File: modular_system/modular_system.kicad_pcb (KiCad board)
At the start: 2 copper layers, 96.8 x 48.5 mm, 12 parts, among them J1 Screw_Terminal_01x02, J2 Conn_01x01_Male, J3 Conn_01x01_Male, J4 Conn_01x01_Male, J5 Conn_01x01_Male, J6 Conn_01x04_Female, J7 Conn_01x04_Female, U1 BluePill_STM32F103C

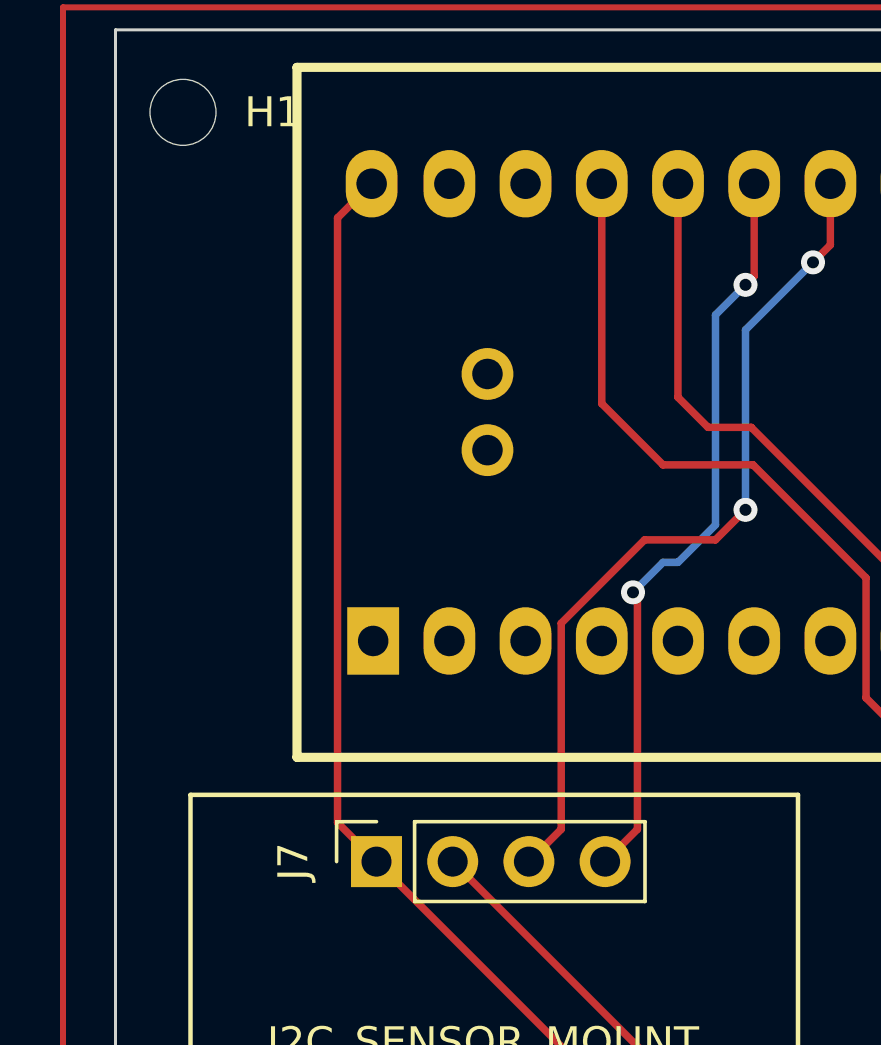
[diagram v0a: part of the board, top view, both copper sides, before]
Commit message: added extra ground trace
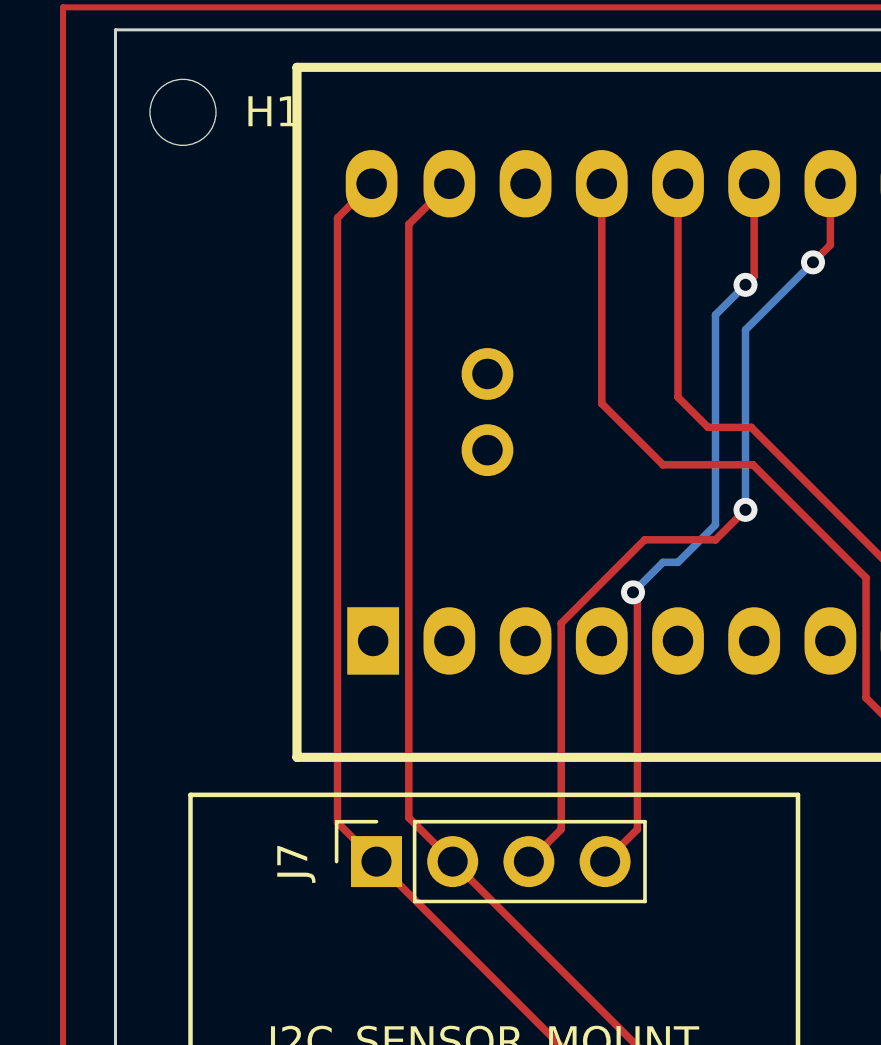
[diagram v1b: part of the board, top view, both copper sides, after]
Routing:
- net GND: track 126.8 -> 150.5 mm
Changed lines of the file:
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@@
   (segment (start 108.901089 56.767311) (end 110.0384 55.63) (width 0.25) (layer "F.Cu") (net 2))
   (segment (start 148.35 88.98) (end 120.955 88.98) (width 0.25) (layer "F.Cu") (net 2))
+  (segment (start 111.277311 56.981889) (end 111.277311 76.762311) (width 0.25) (layer "F.Cu") (net 3))
   (segment (start 134.77 91.52) (end 134.75 91.5) (width 0.25) (layer "F.Cu") (net 3))
   (segment (start 158.3492 75.8492) (end 158.5 76) (width 0.25) (layer "F.Cu") (net 3))
@@
   (segment (start 165.75 81.5) (end 176 71.25) (width 0.25) (layer "F.Cu") (net 3))
   (segment (start 148.35 91.52) (end 155.73 91.52) (width 0.25) (layer "F.Cu") (net 3))
+  (segment (start 112.6292 55.63) (end 111.277311 56.981889) (width 0.25) (layer "F.Cu") (net 3))
+  (segment (start 111.277311 76.762311) (end 112.74 78.225) (width 0.25) (layer "F.Cu") (net 3))
   (segment (start 177.035 56.215) (end 179.055 56.215) (width 0.25) (layer "F.Cu") (net 3))
   (segment (start 165.75 81.5) (end 162 81.5) (width 0.25) (layer "F.Cu") (net 3))

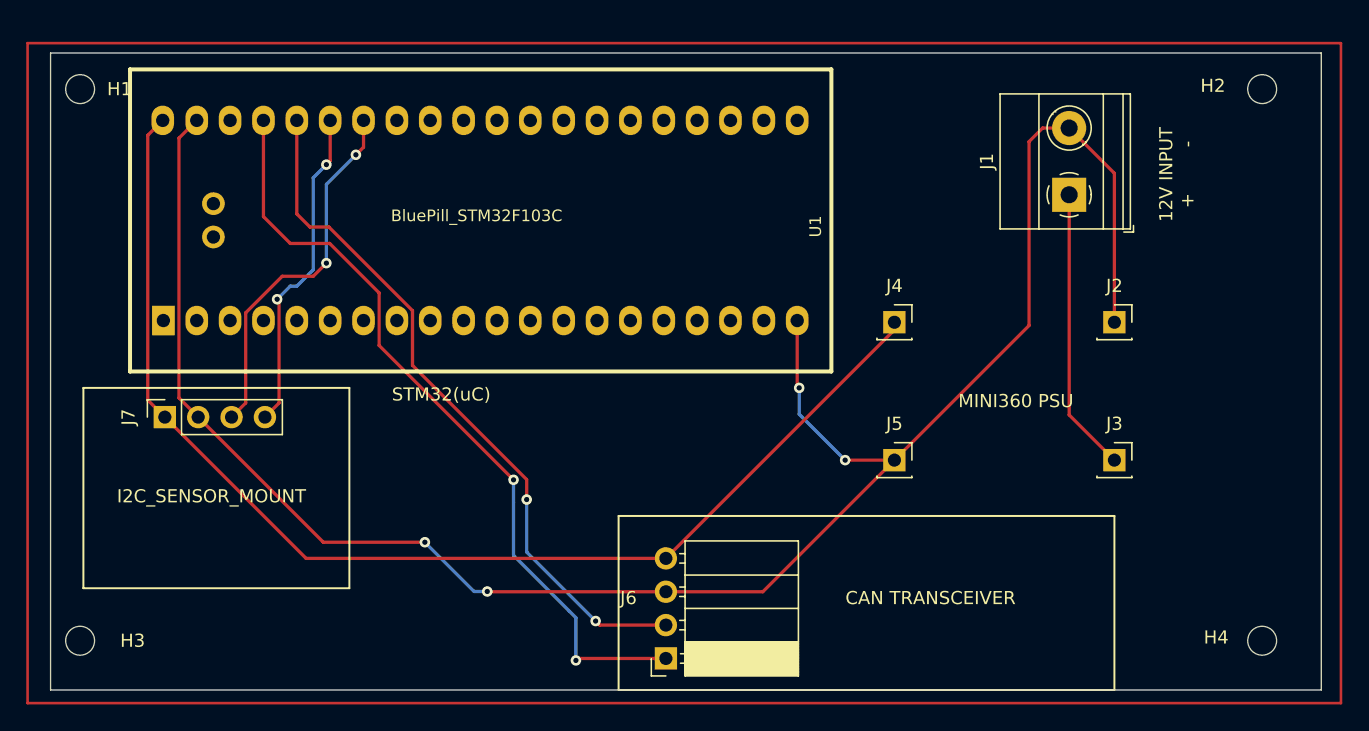
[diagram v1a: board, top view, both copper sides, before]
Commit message: updated with new labels and text on silkscreen
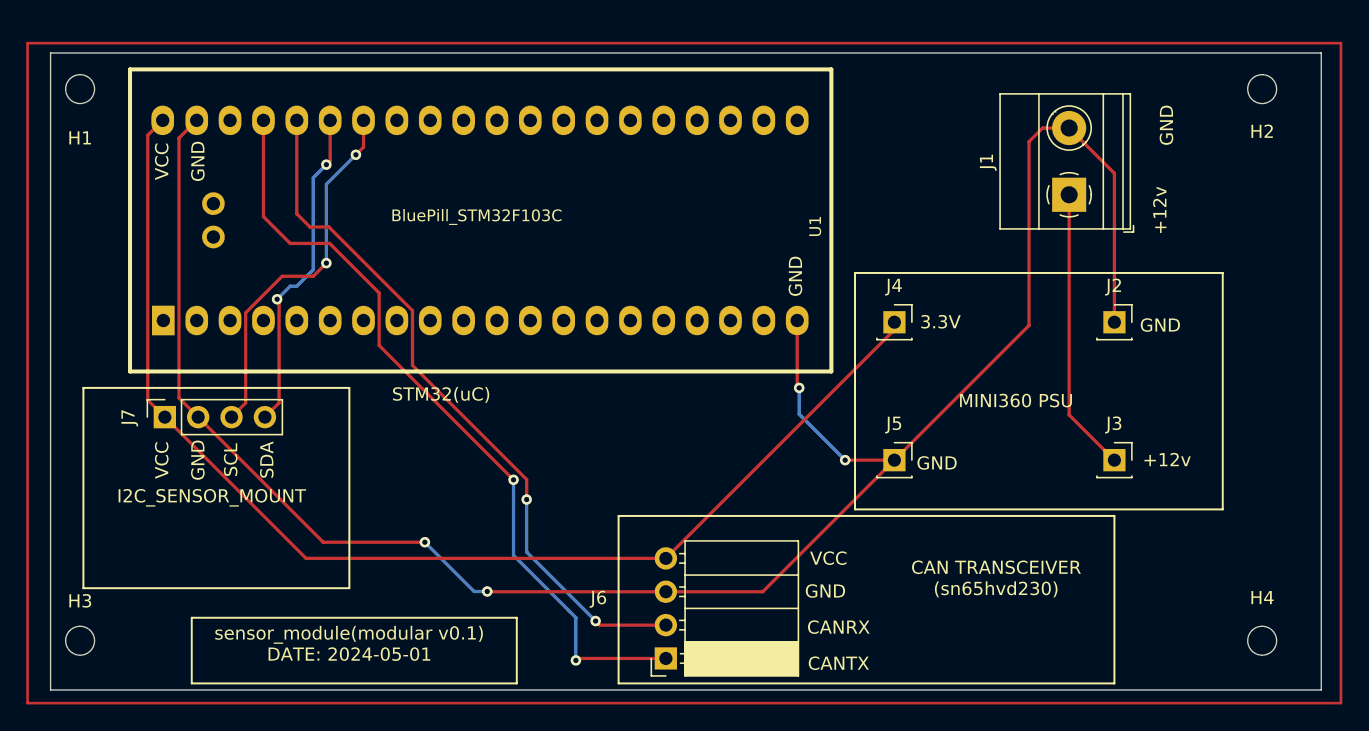
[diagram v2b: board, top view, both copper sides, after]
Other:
- board text added: "+12v"
- board text added: "3.3V"
- board text added: "CAN TRANSCEIVER (sn65hvd230)"
- board text added: "CANRX"
- board text added: "CANTX"
- board text added: "GND"
- board text added: "SCL"
- board text added: "SDA"
- board text added: "VCC"
- board text added: "sensor_module(modular v0.1) DATE: 2024-05-01"
- board text removed: "12V INPUT + -"
- board text removed: "CAN TRANSCEIVER"
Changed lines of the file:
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@@
     (property "Sheetname" "")
     (attr exclude_from_pos_files)
-    (fp_text reference "H4" (at -3.5 -0.25) (layer "F.SilkS")
+    (fp_text reference "H4" (at 0 -3.25) (layer "F.SilkS")
       (effects (font (size 1 1) (thickness 0.15)))
     )
@@
     (property "Sheetname" "")
     (attr through_hole)
-    (fp_text reference "J6" (at 2.85 4.6) (layer "F.SilkS")
+    (fp_text reference "J6" (at 5.1 4.6) (layer "F.SilkS")
       (effects (font (size 1 1) (thickness 0.15)))
     )
@@
     (property "Sheetname" "")
     (attr exclude_from_pos_files)
-    (fp_text reference "H2" (at -3.75 -0.25) (layer "F.SilkS")
+    (fp_text reference "H2" (at 0 3.25) (layer "F.SilkS")
       (effects (font (size 1 1) (thickness 0.15)))
     )
@@
     (property "Sheetname" "")
     (attr exclude_from_pos_files)
-    (fp_text reference "H3" (at 4 0) (layer "F.SilkS")
+    (fp_text reference "H3" (at 0 -3) (layer "F.SilkS")
       (effects (font (size 1 1) (thickness 0.15)))
     )
@@
     (property "Sheetname" "")
     (attr exclude_from_pos_files)
-    (fp_text reference "H1" (at 3 0) (layer "F.SilkS")
+    (fp_text reference "H1" (at 0 3.75) (layer "F.SilkS")
       (effects (font (size 1 1) (thickness 0.15)))
     )
@@
   (gr_rect (start 99.75 49.75) (end 199.75 100) (layer "F.Cu") (width 0.2) (fill none))
   (gr_rect (start 104 76) (end 124.25 91.25) (layer "F.SilkS") (width 0.15) (fill none))
-  (gr_rect (start 144.75 85.75) (end 182.5 99) (layer "F.SilkS") (width 0.15) (fill none))
+  (gr_rect (start 112.25 93.5) (end 137 98.5) (layer "F.SilkS") (width 0.15) (fill none))
+  (gr_rect (start 144.75 85.75) (end 182.5 98.5) (layer "F.SilkS") (width 0.15) (fill none))
+  (gr_rect (start 162.75 67.25) (end 190.75 85.25) (layer "F.SilkS") (width 0.15) (fill none))
   (gr_rect (start 101.5 50.5) (end 198.25 99) (layer "Edge.Cuts") (width 0.1) (fill none))
+  (gr_text "CANTX" (at 161.5 97) (layer "F.SilkS")
+    (effects (font (size 1 1) (thickness 0.15)))
+  )
+  (gr_text "VCC" (at 160.75 89) (layer "F.SilkS")
+    (effects (font (size 1 1) (thickness 0.15)))
+  )
+  (gr_text "GND" (at 169 81.75) (layer "F.SilkS")
+    (effects (font (size 1 1) (thickness 0.15)))
+  )
+  (gr_text "SCL" (at 115.25 81.5 90) (layer "F.SilkS")
+    (effects (font (size 1 1) (thickness 0.15)))
+  )
+  (gr_text "SDA" (at 118 81.5 90) (layer "F.SilkS")
+    (effects (font (size 1 1) (thickness 0.15)))
+  )
+  (gr_text "GND" (at 112.75 58.75 90) (layer "F.SilkS")
+    (effects (font (size 1 1) (thickness 0.15)))
+  )
+  (gr_text "GND" (at 186 71.25) (layer "F.SilkS")
+    (effects (font (size 1 1) (thickness 0.15)))
+  )
+  (gr_text "CANRX" (at 161.5 94.25) (layer "F.SilkS")
+    (effects (font (size 1 1) (thickness 0.15)))
+  )
+  (gr_text "+12v" (at 186 62.5 90) (layer "F.SilkS")
+    (effects (font (size 1 1) (thickness 0.15)))
+  )
+  (gr_text "+12v" (at 186.5 81.5) (layer "F.SilkS")
+    (effects (font (size 1 1) (thickness 0.15)))
+  )
+  (gr_text "GND" (at 112.75 81.5 90) (layer "F.SilkS")
+    (effects (font (size 1 1) (thickness 0.15)))
+  )
+  (gr_text "GND" (at 158.25 67.5 90) (layer "F.SilkS")
+    (effects (font (size 1 1) (thickness 0.15)))
+  )
+  (gr_text "3.3V" (at 169.25 71) (layer "F.SilkS")
+    (effects (font (size 1 1) (thickness 0.15)))
+  )
+  (gr_text "VCC" (at 110 58.75 90) (layer "F.SilkS")
+    (effects (font (size 1 1) (thickness 0.15)))
+  )
   (gr_text "MINI360 PSU" (at 175 77) (layer "F.SilkS")
     (effects (font (size 1 1) (thickness 0.15)))
   )
-  (gr_text "12V INPUT\n+		-" (at 187.25 59.75 90) (layer "F.SilkS")
-    (effects (font (size 1 1) (thickness 0.15)))
-  )
   (gr_text "STM32(uC)" (at 131.25 76.5) (layer "F.SilkS")
     (effects (font (size 1 1) (thickness 0.15)))
   )
-  (gr_text "CAN TRANSCEIVER" (at 168.5 92) (layer "F.SilkS")
+  (gr_text "GND" (at 186.5 56 90) (layer "F.SilkS")
+    (effects (font (size 1 1) (thickness 0.15)))
+  )
+  (gr_text "VCC" (at 110 81.5 90) (layer "F.SilkS")
+    (effects (font (size 1 1) (thickness 0.15)))
+  )
+  (gr_text "CAN TRANSCEIVER\n(sn65hvd230)" (at 173.5 90.5) (layer "F.SilkS")
+    (effects (font (size 1 1) (thickness 0.15)))
+  )
+  (gr_text "GND" (at 160.5 91.5) (layer "F.SilkS")
     (effects (font (size 1 1) (thickness 0.15)))
   )
@@
     (effects (font (size 1 1) (thickness 0.15)))
   )
+  (gr_text "sensor_module(modular v0.1)\nDATE: 2024-05-01" (at 124.25 95.5) (layer "F.SilkS")
+    (effects (font (size 1 1) (thickness 0.15)))
+  )
+  (dimension (type aligned) (layer "F.SilkS")
+    (pts (xy 103.75 53.25) (xy 193.75 53.25))
+    (height -9.5)
+    (gr_text "90.0000 mm" (at 148.75 42.6) (layer "F.SilkS")
+      (effects (font (size 1 1) (thickness 0.15)))
+    )
+    (format (units 3) (units_format 1) (precision 4))
+    (style (thickness 0.15) (arrow_length 1.27) (text_position_mode 0) (extension_height 0.58642) (extension_offset 0.5) keep_text_aligned)
+  )
+  (dimension (type aligned) (layer "F.SilkS")
+    (pts (xy 103.75 95.25) (xy 103.75 53.25))
+    (height -10)
+    (gr_text "42.0000 mm" (at 92.6 74.25 90) (layer "F.SilkS")
+      (effects (font (size 1 1) (thickness 0.15)))
+    )
+    (format (units 3) (units_format 1) (precision 4))
+    (style (thickness 0.15) (arrow_length 1.27) (text_position_mode 0) (extension_height 0.58642) (extension_offset 0.5) keep_text_aligned)
+  )
   (segment (start 179.055 78.055) (end 179.055 61.295) (width 0.25) (layer "F.Cu") (net 1))
